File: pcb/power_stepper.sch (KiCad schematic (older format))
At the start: 40 parts, among them J2 Screw_Terminal, U2 powerSTEP01

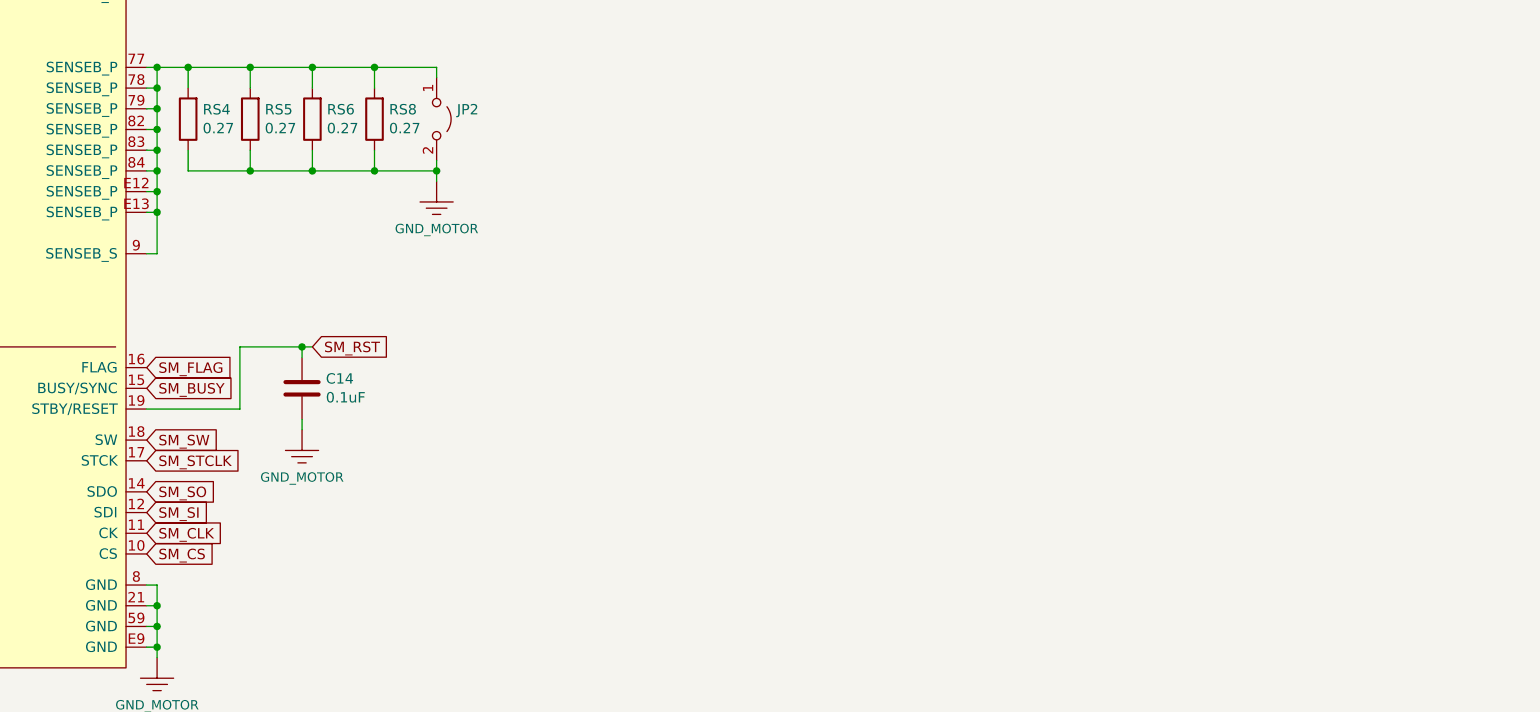
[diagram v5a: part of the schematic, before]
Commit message: ISO7762 added
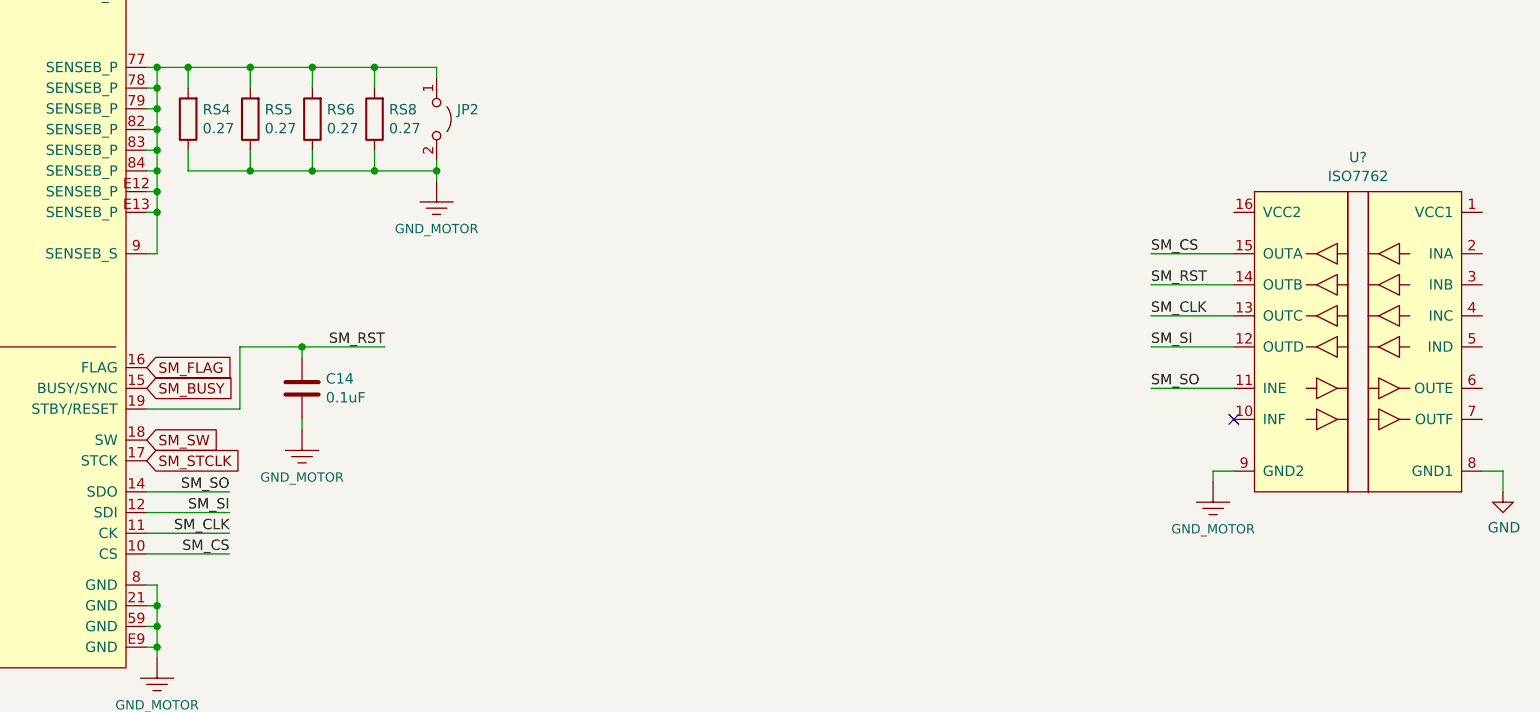
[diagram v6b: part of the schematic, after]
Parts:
- added U?: ISO7762, symbol ISO7762:ISO7762
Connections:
- net 3.3V: now also U?.9 (GND2)
- net SM_CLK: now also U?.13 (OUTC)
- net SM_CS: now also U?.15 (OUTA)
- net SM_RST: now also U?.14 (OUTB)
- net SM_SI: now also U?.12 (OUTD)
- net SM_SO: now also U?.11 (INE)
- new net GND: U?.8 (GND1)
- no-connect marks 2 -> 3
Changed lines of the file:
@@
 Connection ~ 1500 3250
 NoConn ~ 2300 6950
-Text GLabel 3700 6200 2    50   Input ~ 0
-SM_SO
-Text GLabel 3700 6300 2    50   Input ~ 0
-SM_SI
-Text GLabel 3700 6500 2    50   Input ~ 0
-SM_CS
 Wire Wire Line
 	3750 7000 3750 6950
@@
 Text GLabel 3700 6050 2    50   Input ~ 0
 SM_STCLK
-Text GLabel 4500 5500 2    50   Input ~ 0
-SM_RST
 $Comp
 L Device:C C14
@@
 Wire Wire Line
 	3900 4150 4200 4150
-Text GLabel 3700 6400 2    50   Input ~ 0
-SM_CLK
 Wire Wire Line
 	4200 4250 4200 4150
@@
 Connection ~ 4450 5500
 Wire Wire Line
-	4450 5500 4500 5500
-Wire Wire Line
 	4450 5900 4450 5850
 Wire Wire Line
@@
 	1    0    0    -1
 $EndComp
+$Comp
+L ISO7762:ISO7762 U?
+U 1 1 5EAB5353
+P 9550 5450
+F 0 "U?" H 9550 6315 50  0000 C CNN
+F 1 "ISO7762" H 9550 6224 50  0000 C CNN
+F 2 "" H 9050 6200 50  0001 C CNN
+F 3 "" H 9050 6200 50  0001 C CNN
+	1    9550 5450
+	-1   0    0    -1
+$EndComp
+$Comp
+L power:GND #PWR?
+U 1 1 5EB88476
+P 10250 6200
+F 0 "#PWR?" H 10250 5950 50  0001 C CNN
+F 1 "GND" H 10255 6027 50  0000 C CNN
+F 2 "" H 10250 6200 50  0001 C CNN
+F 3 "" H 10250 6200 50  0001 C CNN
+	1    10250 6200
+	1    0    0    -1
+$EndComp
+$Comp
+L ventilator-PowerSymbols:GND_MOTOR #GND?
+U 1 1 5EB8913C
+P 8850 6150
+F 0 "#GND?" H 8900 6100 45  0001 L BNN
+F 1 "GND_MOTOR" H 8850 5920 45  0000 C CNN
+F 2 "XXX-00000" H 8850 5825 60  0001 C CNN
+F 3 "" H 8850 6050 60  0001 C CNN
+	1    8850 6150
+	1    0    0    -1
+$EndComp
+Wire Wire Line
+	10250 6200 10250 6100
+Wire Wire Line
+	10250 6100 10150 6100
+Wire Wire Line
+	8950 6100 8850 6100
+Wire Wire Line
+	8850 6100 8850 6150
+Wire Wire Line
+	8950 5200 8550 5200
+Text Label 8550 5200 0    50   ~ 0
+SM_RST
+Wire Wire Line
+	8950 5350 8550 5350
+Text Label 8550 5350 0    50   ~ 0
+SM_CLK
+Wire Wire Line
+	8950 5500 8550 5500
+Text Label 8550 5500 0    50   ~ 0
+SM_SI
+Wire Wire Line
+	8950 5050 8550 5050
+Text Label 8550 5050 0    50   ~ 0
+SM_CS
+Wire Wire Line
+	8950 5700 8550 5700
+Text Label 8550 5700 0    50   ~ 0
+SM_SO
+NoConn ~ 8950 5850
+Text Label 4850 5500 2    50   ~ 0
+SM_RST
+Wire Wire Line
+	3700 6400 4100 6400
+Wire Wire Line
+	3700 6300 4100 6300
+Text Label 4100 6300 2    50   ~ 0
+SM_SI
+Wire Wire Line
+	3700 6500 4100 6500
+Text Label 4100 6500 2    50   ~ 0
+SM_CS
+Wire Wire Line
+	3700 6200 4100 6200
+Text Label 4100 6200 2    50   ~ 0
+SM_SO
+Text Label 4100 6400 2    50   ~ 0
+SM_CLK
+Wire Wire Line
+	4450 5500 4850 5500
 $EndSCHEMATC

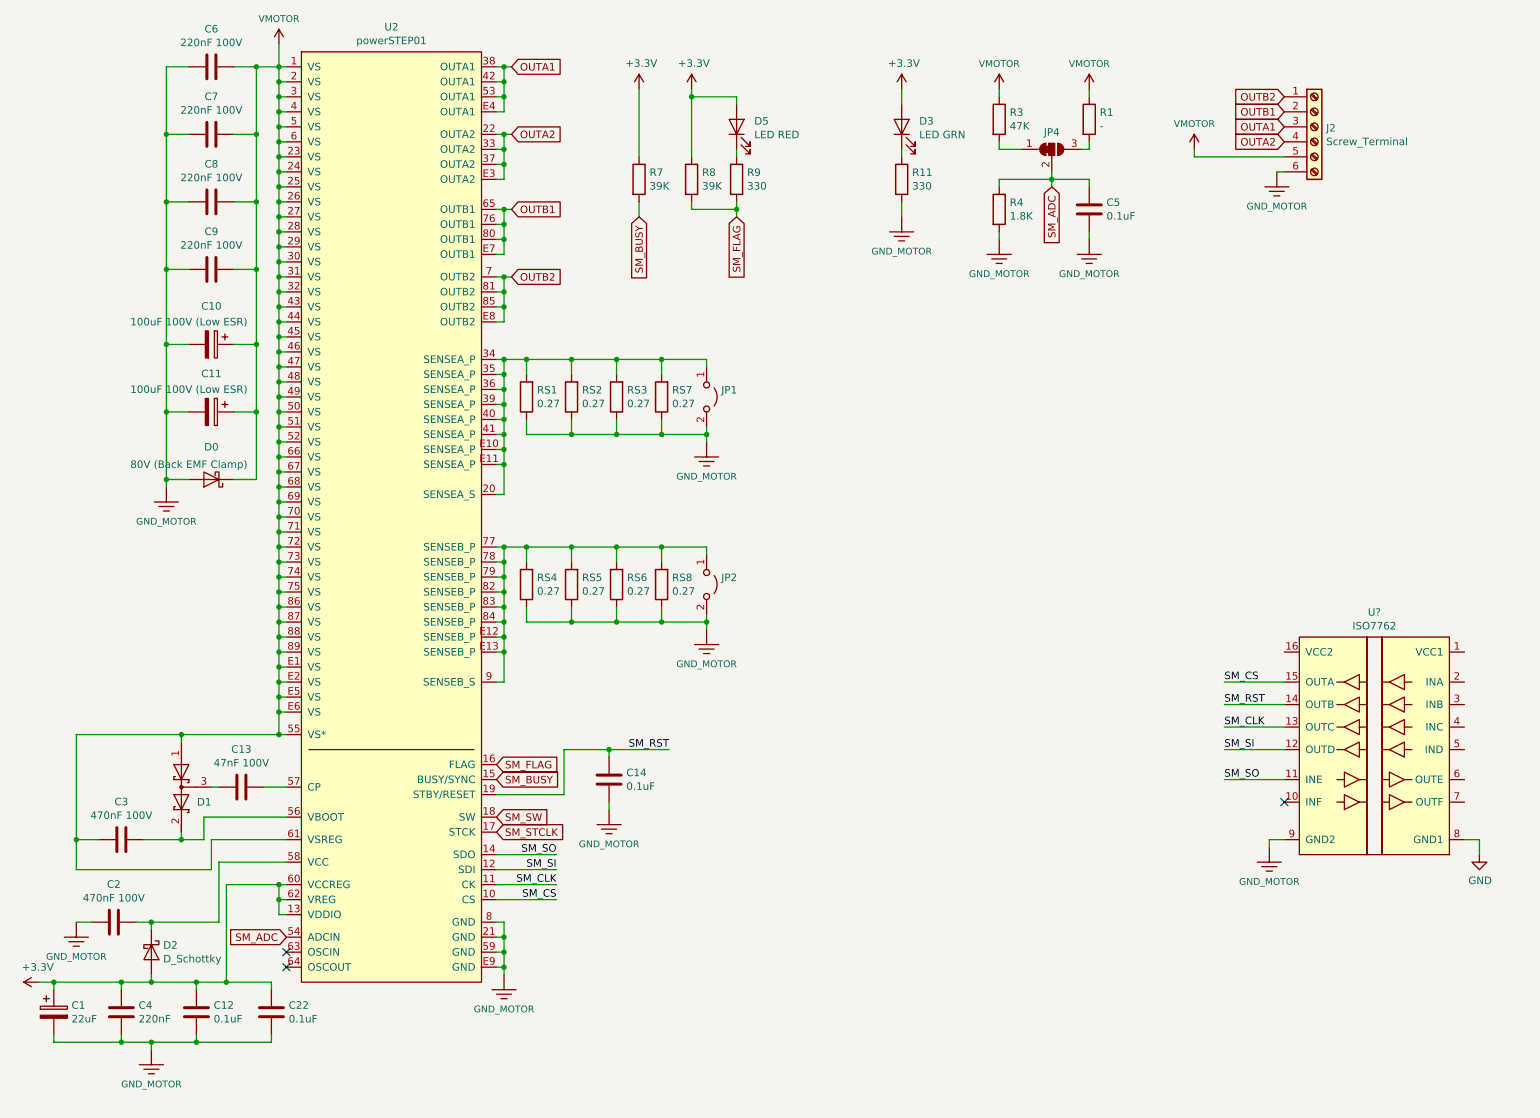
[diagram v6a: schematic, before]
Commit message: UCC12040 added
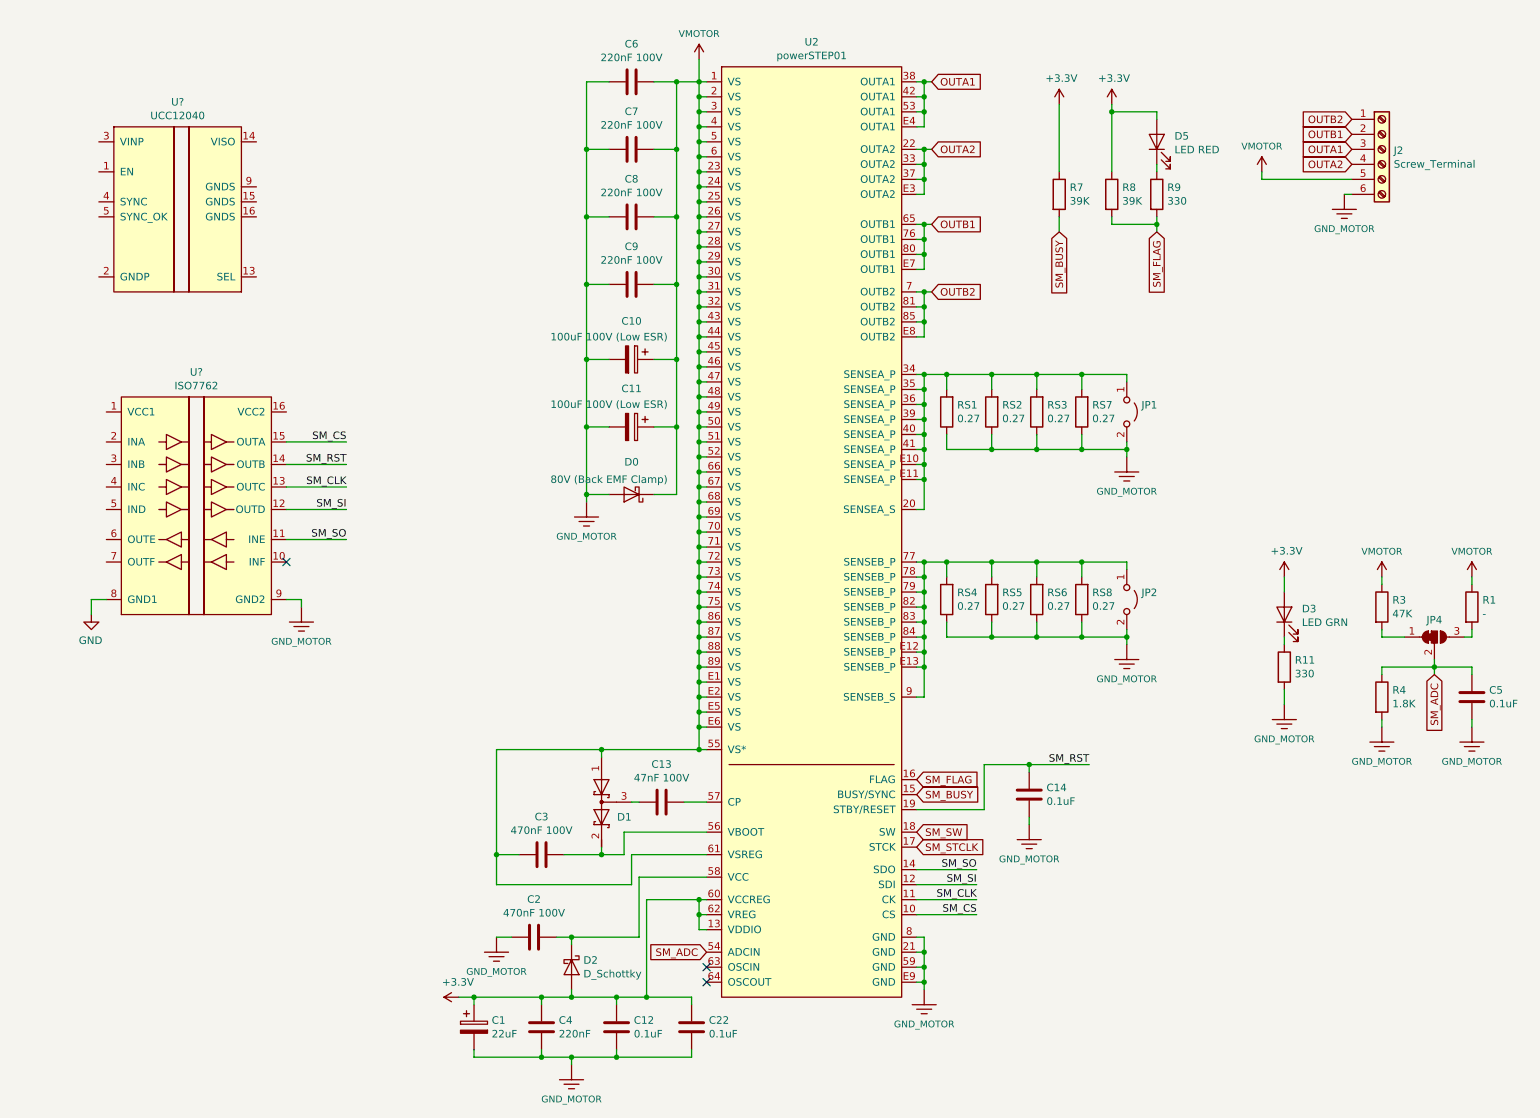
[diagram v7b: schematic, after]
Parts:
- added U?: UCC12040, symbol UCC12040:UCC12040
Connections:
- new net: U?.10 (NC), U?.11 (NC), U?.12 (NC), U?.6 (NC), U?.7 (NC), U?.8 (NC)
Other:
- moved on the sheet: C1, C10, C11, C12, C13, C14, C2, C22, C3, C4, C5, C6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
